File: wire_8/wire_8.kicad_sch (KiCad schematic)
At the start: 2 parts, among them J1 Moat_Wire_16, J2 Moat_Wire_12

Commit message: Wire 8 build
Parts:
- removed J1: Moat_Wire_16, localstuff:Moat_16_2side_HSF, symbol local:Moat_Wire_16
- added J1: Moat_Wire_8, localstuff:Moat_8_2side_HSF, symbol local:Moat_Wire_8
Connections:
- net 12V: now also J1.6 (12V)
- net 24V: now also J1.7 (24V)
- net 5V: now also J1.5 (5V)
- net Bus1: now also J1.2 (Bus1_12)
- net Bus2: now also J1.3 (Bus2_12)
- net Bus3: now also J1.4 (Bus3_12)
- net GND: now also J1.1 (GND)
- net GNDPWR: now also J1.8 (GND_24)
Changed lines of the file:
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@@
   (junction (at 45.72 57.15) (diameter 1.016) (color 0 0 0 0)
   )
-  (junction (at 29.21 43.18) (diameter 1.016) (color 0 0 0 0)
+  (junction (at 53.34 57.15) (diameter 0) (color 0 0 0 0)
   )
-  (junction (at 27.94 50.8) (diameter 1.016) (color 0 0 0 0)
-  )
-  (junction (at 29.21 38.1) (diameter 1.016) (color 0 0 0 0)
-  )
-  (junction (at 53.34 57.15) (diameter 1.016) (color 0 0 0 0)
-  )
-  (junction (at 40.64 40.64) (diameter 1.016) (color 0 0 0 0)
-  )
-  (junction (at 29.21 25.4) (diameter 1.016) (color 0 0 0 0)
-  )
-  (junction (at 38.1 45.72) (diameter 1.016) (color 0 0 0 0)
-  )
-  (junction (at 43.18 35.56) (diameter 1.016) (color 0 0 0 0)
-  )
-  (junction (at 29.21 53.34) (diameter 1.016) (color 0 0 0 0)
-  )
-  (junction (at 29.21 48.26) (diameter 1.016) (color 0 0 0 0)
-  )
-  (wire (pts (xy 29.21 25.4) (xy 66.04 25.4))
-    (stroke (width 0) (type solid) (color 0 0 0 0))
-  )
-  (wire (pts (xy 38.1 45.72) (xy 22.86 45.72))
-    (stroke (width 0) (type solid) (color 0 0 0 0))
-  )
-  (wire (pts (xy 22.86 53.34) (xy 29.21 53.34))
-    (stroke (width 0) (type solid) (color 0 0 0 0))
-  )
-  (wire (pts (xy 29.21 48.26) (xy 29.21 43.18))
-    (stroke (width 0) (type solid) (color 0 0 0 0))
-  )
-  (wire (pts (xy 22.86 43.18) (xy 29.21 43.18))
-    (stroke (width 0) (type solid) (color 0 0 0 0))
-  )
-  (wire (pts (xy 22.86 55.88) (xy 27.94 55.88))
+  (wire (pts (xy 43.18 43.18) (xy 43.18 62.23))
     (stroke (width 0) (type solid) (color 0 0 0 0))
   )
@@
     (stroke (width 0) (type solid) (color 0 0 0 0))
   )
-  (wire (pts (xy 46.99 40.64) (xy 40.64 40.64))
-    (stroke (width 0) (type solid) (color 0 0 0 0))
-  )
-  (wire (pts (xy 29.21 48.26) (xy 53.34 48.26))
-    (stroke (width 0) (type solid) (color 0 0 0 0))
-  )
-  (wire (pts (xy 29.21 58.42) (xy 29.21 53.34))
-    (stroke (width 0) (type solid) (color 0 0 0 0))
-  )
-  (wire (pts (xy 68.58 60.96) (xy 50.8 60.96))
-    (stroke (width 0) (type solid) (color 0 0 0 0))
-  )
-  (wire (pts (xy 48.26 62.23) (xy 48.26 58.42))
-    (stroke (width 0) (type solid) (color 0 0 0 0))
+  (wire (pts (xy 22.86 45.72) (xy 48.26 45.72))
+    (stroke (width 0) (type default) (color 0 0 0 0))
   )
   (wire (pts (xy 53.34 62.23) (xy 53.34 57.15))
     (stroke (width 0) (type solid) (color 0 0 0 0))
   )
+  (wire (pts (xy 38.1 38.1) (xy 38.1 62.23))
+    (stroke (width 0) (type default) (color 0 0 0 0))
+  )
+  (wire (pts (xy 53.34 35.56) (xy 53.34 57.15))
+    (stroke (width 0) (type default) (color 0 0 0 0))
+  )
   (wire (pts (xy 45.72 62.23) (xy 45.72 57.15))
     (stroke (width 0) (type solid) (color 0 0 0 0))
   )
-  (wire (pts (xy 38.1 62.23) (xy 38.1 45.72))
-    (stroke (width 0) (type solid) (color 0 0 0 0))
-  )
-  (wire (pts (xy 44.45 35.56) (xy 43.18 35.56))
-    (stroke (width 0) (type solid) (color 0 0 0 0))
+  (wire (pts (xy 22.86 35.56) (xy 53.34 35.56))
+    (stroke (width 0) (type default) (color 0 0 0 0))
   )
   (wire (pts (xy 35.56 62.23) (xy 35.56 57.15))
     (stroke (width 0) (type solid) (color 0 0 0 0))
   )
-  (wire (pts (xy 22.86 20.32) (xy 60.96 20.32))
-    (stroke (width 0) (type solid) (color 0 0 0 0))
+  (wire (pts (xy 22.86 43.18) (xy 43.18 43.18))
+    (stroke (width 0) (type default) (color 0 0 0 0))
   )
-  (wire (pts (xy 29.21 30.48) (xy 22.86 30.48))
-    (stroke (width 0) (type solid) (color 0 0 0 0))
+  (wire (pts (xy 22.86 40.64) (xy 40.64 40.64))
+    (stroke (width 0) (type default) (color 0 0 0 0))
   )
-  (wire (pts (xy 49.53 45.72) (xy 38.1 45.72))
-    (stroke (width 0) (type solid) (color 0 0 0 0))
+  (wire (pts (xy 50.8 48.26) (xy 50.8 62.23))
+    (stroke (width 0) (type default) (color 0 0 0 0))
   )
-  (wire (pts (xy 22.86 22.86) (xy 63.5 22.86))
-    (stroke (width 0) (type solid) (color 0 0 0 0))
+  (wire (pts (xy 22.86 48.26) (xy 50.8 48.26))
+    (stroke (width 0) (type default) (color 0 0 0 0))
   )
-  (wire (pts (xy 43.18 35.56) (xy 43.18 62.23))
-    (stroke (width 0) (type solid) (color 0 0 0 0))
-  )
-  (wire (pts (xy 22.86 27.94) (xy 68.58 27.94))
-    (stroke (width 0) (type solid) (color 0 0 0 0))
-  )
-  (wire (pts (xy 22.86 38.1) (xy 29.21 38.1))
-    (stroke (width 0) (type solid) (color 0 0 0 0))
-  )
-  (wire (pts (xy 50.8 60.96) (xy 50.8 62.23))
-    (stroke (width 0) (type solid) (color 0 0 0 0))
-  )
-  (wire (pts (xy 29.21 53.34) (xy 55.88 53.34))
-    (stroke (width 0) (type solid) (color 0 0 0 0))
-  )
-  (wire (pts (xy 22.86 48.26) (xy 29.21 48.26))
-    (stroke (width 0) (type solid) (color 0 0 0 0))
-  )
-  (wire (pts (xy 22.86 25.4) (xy 29.21 25.4))
-    (stroke (width 0) (type solid) (color 0 0 0 0))
-  )
-  (wire (pts (xy 66.04 58.42) (xy 66.04 25.4))
-    (stroke (width 0) (type solid) (color 0 0 0 0))
-  )
-  (wire (pts (xy 29.21 33.02) (xy 22.86 33.02))
-    (stroke (width 0) (type solid) (color 0 0 0 0))
-  )
-  (wire (pts (xy 27.94 55.88) (xy 27.94 50.8))
-    (stroke (width 0) (type solid) (color 0 0 0 0))
-  )
-  (wire (pts (xy 48.26 58.42) (xy 66.04 58.42))
-    (stroke (width 0) (type solid) (color 0 0 0 0))
-  )
-  (wire (pts (xy 27.94 50.8) (xy 22.86 50.8))
+  (wire (pts (xy 22.86 53.34) (xy 55.88 53.34))
     (stroke (width 0) (type solid) (color 0 0 0 0))
   )
@@
     (stroke (width 0) (type solid) (color 0 0 0 0))
   )
-  (wire (pts (xy 27.94 50.8) (xy 58.42 50.8))
-    (stroke (width 0) (type solid) (color 0 0 0 0))
-  )
-  (wire (pts (xy 60.96 20.32) (xy 60.96 62.23))
+  (wire (pts (xy 22.86 50.8) (xy 58.42 50.8))
     (stroke (width 0) (type solid) (color 0 0 0 0))
   )
@@
     (stroke (width 0) (type solid) (color 0 0 0 0))
   )
-  (wire (pts (xy 22.86 58.42) (xy 29.21 58.42))
-    (stroke (width 0) (type solid) (color 0 0 0 0))
+  (wire (pts (xy 48.26 45.72) (xy 48.26 62.23))
+    (stroke (width 0) (type default) (color 0 0 0 0))
   )
-  (wire (pts (xy 29.21 43.18) (xy 29.21 38.1))
-    (stroke (width 0) (type solid) (color 0 0 0 0))
-  )
-  (wire (pts (xy 29.21 38.1) (xy 29.21 33.02))
-    (stroke (width 0) (type solid) (color 0 0 0 0))
-  )
-  (wire (pts (xy 29.21 25.4) (xy 29.21 30.48))
-    (stroke (width 0) (type solid) (color 0 0 0 0))
-  )
-  (wire (pts (xy 40.64 40.64) (xy 22.86 40.64))
-    (stroke (width 0) (type solid) (color 0 0 0 0))
-  )
-  (wire (pts (xy 68.58 27.94) (xy 68.58 60.96))
-    (stroke (width 0) (type solid) (color 0 0 0 0))
-  )
-  (wire (pts (xy 63.5 22.86) (xy 63.5 62.23))
-    (stroke (width 0) (type solid) (color 0 0 0 0))
-  )
-  (wire (pts (xy 43.18 35.56) (xy 22.86 35.56))
-    (stroke (width 0) (type solid) (color 0 0 0 0))
-  )
-  (wire (pts (xy 53.34 57.15) (xy 53.34 48.26))
-    (stroke (width 0) (type solid) (color 0 0 0 0))
+  (wire (pts (xy 22.86 38.1) (xy 38.1 38.1))
+    (stroke (width 0) (type default) (color 0 0 0 0))
   )
   (wire (pts (xy 55.88 53.34) (xy 55.88 62.23))
     (stroke (width 0) (type solid) (color 0 0 0 0))
   )
-  (label "GND" (at 52.07 48.26 0)
+  (label "GND" (at 53.34 57.15 0)
     (effects (font (size 1.27 1.27)) (justify left bottom))
   )
-  (label "Bus1" (at 44.45 45.72 0)
+  (label "Bus1" (at 38.1 38.1 0)
     (effects (font (size 1.27 1.27)) (justify left bottom))
   )
-  (label "5V" (at 41.91 25.4 0)
+  (label "5V" (at 48.26 45.72 0)
     (effects (font (size 1.27 1.27)) (justify left bottom))
   )
-  (label "12V" (at 39.37 27.94 0)
+  (label "Bus2" (at 40.64 40.64 0)
     (effects (font (size 1.27 1.27)) (justify left bottom))
   )
-  (label "Bus2" (at 44.45 40.64 0)
-    (effects (font (size 1.27 1.27)) (justify left bottom))
-  )
-  (label "Bus3" (at 44.45 35.56 0)
+  (label "Bus3" (at 43.18 43.18 0)
     (effects (font (size 1.27 1.27)) (justify left bottom))
   )
@@
     (effects (font (size 1.27 1.27)) (justify left bottom))
   )
+  (label "12V" (at 50.8 48.26 0)
+    (effects (font (size 1.27 1.27)) (justify left bottom))
+  )
   (label "GNDPWR" (at 29.21 53.34 0)
     (effects (font (size 1.27 1.27)) (justify left bottom))
-  )
-  (symbol (lib_id "local:Moat_Wire_16") (at 17.78 38.1 0) (mirror y) (unit 1)
-    (in_bom yes) (on_board yes)
-    (property "Reference" "J1" (id 0) (at 16.1798 14.605 0))
-    (property "Value" "Moat_Wire_16" (id 1) (at 16.1798 16.9164 0))
-    (property "Footprint" "localstuff:Moat_16_2side_HSF" (id 2) (at 17.78 63.5 0)
-      (effects (font (size 1.27 1.27)) hide)
-    )
-    (property "Datasheet" "" (id 3) (at 17.78 38.1 0)
-      (effects (font (size 1.27 1.27)) hide)
-    )
-    (property "Digikey" "478-6173-1-ND *2" (id 4) (at 17.78 15.24 0)
-      (effects (font (size 1.27 1.27)) hide)
-    )
-    (pin "1")
-    (pin "10")
-    (pin "11")
-    (pin "12")
-    (pin "13")
-    (pin "14")
-    (pin "15")
-    (pin "16")
-    (pin "2")
-    (pin "3")
-    (pin "4")
-    (pin "5")
-    (pin "6")
-    (pin "7")
-    (pin "8")
-    (pin "9")
   )
   (symbol (lib_id "local:Moat_Wire_12") (at 58.42 67.31 90) (mirror x) (unit 1)
@@
     (pin "9")
   )
+  (symbol (lib_id "local:Moat_Wire_8") (at 17.78 48.26 0) (mirror y) (unit 1)
+    (in_bom yes) (on_board yes) (fields_autoplaced)
+    (property "Reference" "J1" (id 0) (at 18.415 30.48 0))
+    (property "Value" "Moat_Wire_8" (id 1) (at 18.415 33.02 0))
+    (property "Footprint" "localstuff:Moat_8_2side_HSF" (id 2) (at 21.59 58.42 0)
+      (effects (font (size 1.27 1.27)) hide)
+    )
+    (property "Datasheet" "" (id 3) (at 17.78 45.72 0)
+      (effects (font (size 1.27 1.27)) hide)
+    )
+    (pin "1")
+    (pin "2")
+    (pin "3")
+    (pin "4")
+    (pin "5")
+    (pin "6")
+    (pin "7")
+    (pin "8")
+  )
   (sheet_instances
     (path "/" (page "1"))
   )
   (symbol_instances
-    (path "/00000000-0000-0000-0000-00005cbe90b4"
-      (reference "J1") (unit 1) (value "Moat_Wire_16") (footprint "localstuff:Moat_16_2side_HSF")
+    (path "/811d06c8-e35a-4323-8e51-11882cc1e2ee"
+      (reference "J1") (unit 1) (value "Moat_Wire_8") (footprint "localstuff:Moat_8_2side_HSF")
     )
     (path "/00000000-0000-0000-0000-0000612c2531"

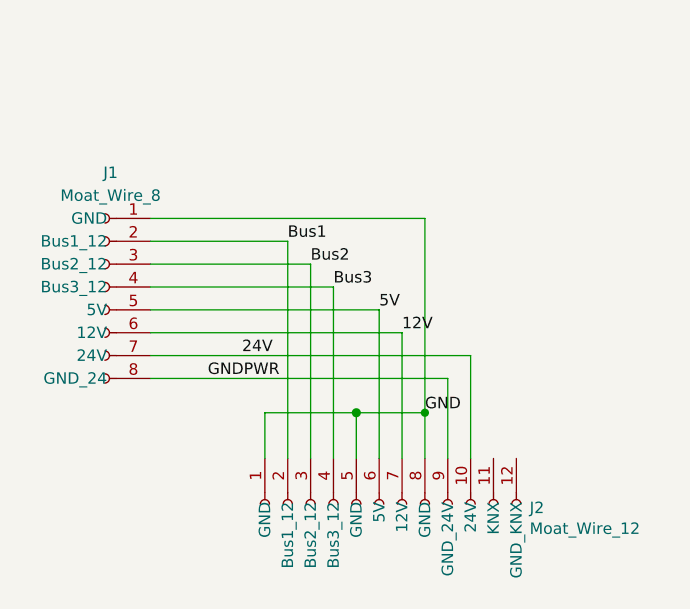
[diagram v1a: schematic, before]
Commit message: Plug updates
drop in/out from plug24
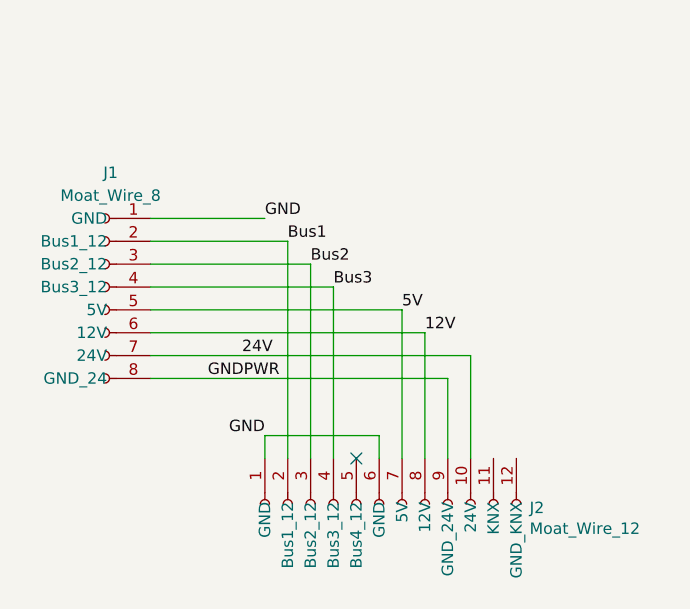
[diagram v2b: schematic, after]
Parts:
- J2: symbol local:Moat_Wire_12 -> localstuff:Moat_Wire_12
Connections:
- net 12V: now also J2.8 (12V); no longer J2.7 (12V)
- net 5V: now also J2.7 (5V); no longer J2.6 (5V)
- net GND: now also J2.6 (GND); no longer J2.5 (GND), J2.8 (GND)
- no-connect marks 0 -> 1
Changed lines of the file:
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@@
 (kicad_sch (version 20211123) (generator eeschema)
   (paper "A4")
-  (junction (at 45.72 57.15) (diameter 1.016) (color 0 0 0 0)
-  )
-  (junction (at 53.34 57.15) (diameter 0) (color 0 0 0 0)
-  )
+  (no_connect (at 45.72 62.23))
   (wire (pts (xy 43.18 43.18) (xy 43.18 62.23))
     (stroke (width 0) (type solid) (color 0 0 0 0))
@@
     (stroke (width 0) (type solid) (color 0 0 0 0))
   )
-  (wire (pts (xy 35.56 57.15) (xy 45.72 57.15))
-    (stroke (width 0) (type solid) (color 0 0 0 0))
-  )
-  (wire (pts (xy 22.86 45.72) (xy 48.26 45.72))
+  (wire (pts (xy 53.34 48.26) (xy 53.34 62.23))
     (stroke (width 0) (type default) (color 0 0 0 0))
   )
-  (wire (pts (xy 53.34 62.23) (xy 53.34 57.15))
-    (stroke (width 0) (type solid) (color 0 0 0 0))
+  (wire (pts (xy 22.86 48.26) (xy 53.34 48.26))
+    (stroke (width 0) (type default) (color 0 0 0 0))
   )
   (wire (pts (xy 38.1 38.1) (xy 38.1 62.23))
     (stroke (width 0) (type default) (color 0 0 0 0))
   )
-  (wire (pts (xy 53.34 35.56) (xy 53.34 57.15))
+  (wire (pts (xy 48.26 59.69) (xy 35.56 59.69))
     (stroke (width 0) (type default) (color 0 0 0 0))
   )
-  (wire (pts (xy 45.72 62.23) (xy 45.72 57.15))
-    (stroke (width 0) (type solid) (color 0 0 0 0))
-  )
-  (wire (pts (xy 22.86 35.56) (xy 53.34 35.56))
+  (wire (pts (xy 48.26 62.23) (xy 48.26 59.69))
     (stroke (width 0) (type default) (color 0 0 0 0))
   )
-  (wire (pts (xy 35.56 62.23) (xy 35.56 57.15))
+  (wire (pts (xy 35.56 62.23) (xy 35.56 59.69))
     (stroke (width 0) (type solid) (color 0 0 0 0))
   )
@@
     (stroke (width 0) (type default) (color 0 0 0 0))
   )
-  (wire (pts (xy 50.8 48.26) (xy 50.8 62.23))
-    (stroke (width 0) (type default) (color 0 0 0 0))
-  )
-  (wire (pts (xy 22.86 48.26) (xy 50.8 48.26))
-    (stroke (width 0) (type default) (color 0 0 0 0))
-  )
   (wire (pts (xy 22.86 53.34) (xy 55.88 53.34))
     (stroke (width 0) (type solid) (color 0 0 0 0))
   )
-  (wire (pts (xy 45.72 57.15) (xy 53.34 57.15))
-    (stroke (width 0) (type solid) (color 0 0 0 0))
+  (wire (pts (xy 50.8 45.72) (xy 50.8 62.23))
+    (stroke (width 0) (type default) (color 0 0 0 0))
   )
   (wire (pts (xy 22.86 50.8) (xy 58.42 50.8))
@@
     (stroke (width 0) (type solid) (color 0 0 0 0))
   )
-  (wire (pts (xy 48.26 45.72) (xy 48.26 62.23))
+  (wire (pts (xy 22.86 35.56) (xy 35.56 35.56))
+    (stroke (width 0) (type default) (color 0 0 0 0))
+  )
+  (wire (pts (xy 22.86 45.72) (xy 50.8 45.72))
     (stroke (width 0) (type default) (color 0 0 0 0))
   )
@@
     (stroke (width 0) (type solid) (color 0 0 0 0))
   )
-  (label "GND" (at 53.34 57.15 0)
+  (label "GND" (at 35.56 35.56 0)
     (effects (font (size 1.27 1.27)) (justify left bottom))
+  )
+  (label "GND" (at 35.56 59.69 180)
+    (effects (font (size 1.27 1.27)) (justify right bottom))
   )
   (label "Bus1" (at 38.1 38.1 0)
     (effects (font (size 1.27 1.27)) (justify left bottom))
   )
-  (label "5V" (at 48.26 45.72 0)
+  (label "5V" (at 50.8 45.72 0)
     (effects (font (size 1.27 1.27)) (justify left bottom))
   )
@@
     (effects (font (size 1.27 1.27)) (justify left bottom))
   )
-  (label "12V" (at 50.8 48.26 0)
+  (label "12V" (at 53.34 48.26 0)
     (effects (font (size 1.27 1.27)) (justify left bottom))
   )
@@
     (effects (font (size 1.27 1.27)) (justify left bottom))
   )
-  (symbol (lib_id "local:Moat_Wire_12") (at 58.42 67.31 90) (mirror x) (unit 1)
+  (symbol (lib_id "localstuff:Moat_Wire_12") (at 58.42 67.31 90) (mirror x) (unit 1)
     (in_bom yes) (on_board yes)
     (property "Reference" "J2" (id 0) (at 64.9732 67.7164 90)
